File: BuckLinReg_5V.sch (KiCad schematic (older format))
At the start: 41 parts, among them J1 Barrel_Jack, J2 Conn_01x02_Male, J3 Conn_01x02_Male, J4 Conn_01x02_Male, Q1 SQD40061EL, U1 TPS56339DDC, U2 LM1085-5.0

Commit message: Added overcurrent protection circuit and assigned all MFPNs and footprints
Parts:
- added C12, C13, C14, C4: 0.1u, Capacitor_SMD:C_0603_1608Metric_Pad1.08x0.95mm_HandSolder, symbol Device:C_Small
- added D4: 3.0, Diode_SMD:D_SOD-323, symbol Device:D_Zener
- added D5: YELLOW, Diode_SMD:D_1206_3216Metric_Pad1.42x1.75mm_HandSolder, symbol Device:LED
- added Q1: PMBT2222, Package_TO_SOT_SMD:SOT-23_Handsoldering, symbol Device:Q_NPN_BEC
- added R10, R18, R2: 10k, Resistor_SMD:R_1206_3216Metric_Pad1.30x1.75mm_HandSolder, symbol Device:R
- added R11, R12: 1k, Resistor_SMD:R_1206_3216Metric_Pad1.30x1.75mm_HandSolder, symbol Device:R
- added R13, R14, R16: 100k, Resistor_SMD:R_1206_3216Metric_Pad1.30x1.75mm_HandSolder, symbol Device:R
- added R17: 12k, Resistor_SMD:R_1206_3216Metric_Pad1.30x1.75mm_HandSolder, symbol Device:R
- added SW1: SW_SPDT, Connector_PinHeader_2.54mm:PinHeader_1x03_P2.54mm_Vertical, symbol Switch:SW_SPDT
- added U1: TLV76050DBZT, Package_TO_SOT_SMD:SOT-23_Handsoldering, symbol BuckLinReg_5V:TLV76050DBZT
- added U2: LMV358, Package_SO:SOIC-8_3.9x4.9mm_P1.27mm, symbol Amplifier_Operational:LMV358
- added U3: 74HCT00, Package_SO:SOIC-14_3.9x8.7mm_P1.27mm, symbol 74xx:74LS00
- added U4: SN74HCT02, Package_SO:SOIC-14_3.9x8.7mm_P1.27mm, symbol 74xx:74LS02
- added U5: TCM810, Package_TO_SOT_SMD:SOT-23_Handsoldering, symbol Power_Supervisor:TCM810
- J2: renamed from J3; value Conn_01x02_Male -> 1x2 Male
- J3: renamed from J4; value Conn_01x02_Male -> 1x2 Male
- J4: renamed from J2; value Conn_01x02_Male -> 1x2 Male
- R8: renamed from R6; value 36k -> 68k; MFPN RMCF1206FT36K0 -> RMCF1206JT68K0
- R9: renamed from R7; value 4.7k -> 33k; MFPN RMCF1206FT4K70 -> RMCF1206JT33K0
- U7: renamed from U2; value LM1085-5.0 -> LM1084-5.0
- renumbered C9 to C10, C10 to C11, C4 to C5, C5 to C6, C6 to C7, C7 to C8, C8 to C9, D3 to D1, D1 to D3, Q1 to Q2, R8 to R1, R9 to R15, R1 to R3, R2 to R4, R4 to R5, R5 to R6, R3 to R7, TP2 to TP1, TP3 to TP2, TP1 to TP3, U1 to U6
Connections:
- net labels added: +Vin, 5V0_LOGIC, 5V0_Out, OCP_TRIGGER, POR, Q, S, SR+, SR-, SW_SIG, Vo, ~PWR_EN, ~Q, ~SW_SIG
- net labels removed: CapNode, U1Vin, U2Vin, Vout
- wire segments 121 -> 238
- no-connect marks 0 -> 2
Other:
- note added: "R"
- note added: "S"
- note added: "TPS56339 has a 5 ms soft-start\nWe must assert a definite EN voltage by t = 2 ms after power-up"
- note added: "Vo= (100k/1k) * ( (SR+) - (SR-) )"
- moved on the sheet: C1, C10, C11, C2, C3, C5, C6, C7, C8, C9, D1, D2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

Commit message: Two grounds: GNDA and pwrGND.  Continued PCB dev.
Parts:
- added NT1: Net-Tie_2, NetTie:NetTie-2_SMD_Pad0.5mm, symbol Device:Net-Tie_2
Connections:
- net labels added: DFA+, DFA-, GNDA, GNDPWR
- wire segments 238 -> 241
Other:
- moved on the sheet: R11, R12

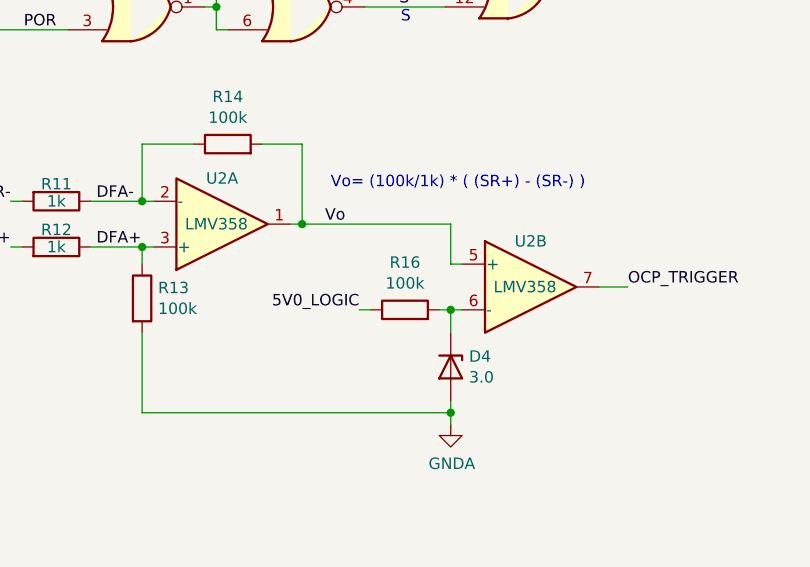
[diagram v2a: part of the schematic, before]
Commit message: Simulated zener for different values R.  Routed logic portion of board.
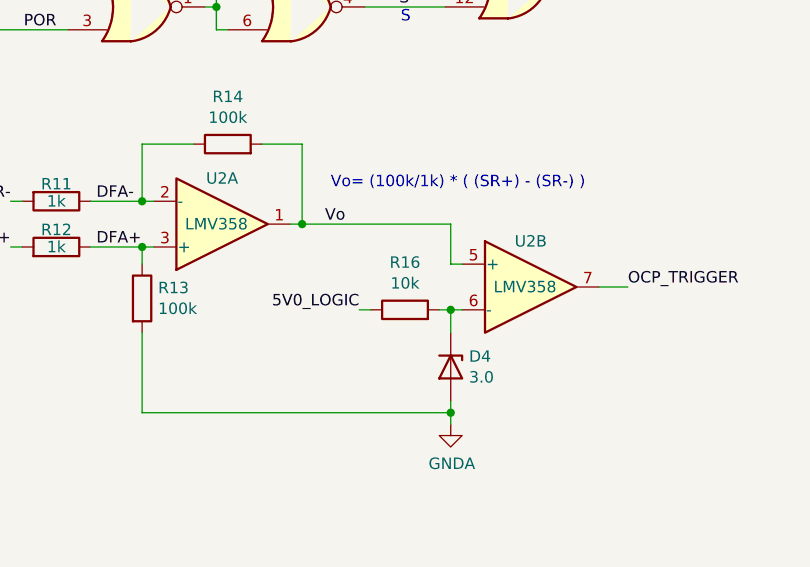
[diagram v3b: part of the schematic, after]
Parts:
- R16: value 100k -> 10k; MFPN RMCF1206JG100K -> RMCF1206JT10K0
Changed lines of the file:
@@
 P 7175 9250
 F 0 "R16" V 7382 9250 50  0000 C CNN
-F 1 "100k" V 7291 9250 50  0000 C CNN
+F 1 "10k" V 7291 9250 50  0000 C CNN
 F 2 "Resistor_SMD:R_1206_3216Metric_Pad1.30x1.75mm_HandSolder" V 7105 9250 50  0001 C CNN
 F 3 "~" H 7175 9250 50  0001 C CNN
-F 4 "RMCF1206JG100K" H 7175 9250 50  0001 C CNN "MFPN"
+F 4 "RMCF1206JT10K0" H 7175 9250 50  0001 C CNN "MFPN"
 	1    7175 9250
 	0    -1   -1   0
@@
 F 1 "LM1084-5.0" H 10500 4301 50  0000 C CNN
 F 2 "Package_TO_SOT_SMD:TO-263-3_TabPin2" H 10500 4400 50  0001 C CIN
-F 3 "http://www.ti.com/lit/ds/symlink/lm1085.pdf" H 10500 4150 50  0001 C CNN
+F 3 "http://www.ti.com/general/docs/suppproductinfo.tsp?distId=10&gotoUrl=http%3A%2F%2Fwww.ti.com%2Flit%2Fgpn%2Flm1084" H 10500 4150 50  0001 C CNN
 F 4 "LM1084ISX-5.0/NOPB" H 10500 4150 50  0001 C CNN "MFPN"
 	1    10500 4150
@@
 $EndComp
 $Comp
-L power:GNDA #PWR?
+L power:GNDA #PWR0106
 U 1 1 60668381
 P 2700 10075
-F 0 "#PWR?" H 2700 9825 50  0001 C CNN
+F 0 "#PWR0106" H 2700 9825 50  0001 C CNN
 F 1 "GNDA" H 2705 9902 50  0000 C CNN
 F 2 "" H 2700 10075 50  0001 C CNN
@@
 $EndComp
 $Comp
-L power:GNDA #PWR?
+L power:GNDA #PWR0108
 U 1 1 60698D68
 P 7975 6775
-F 0 "#PWR?" H 7975 6525 50  0001 C CNN
+F 0 "#PWR0108" H 7975 6525 50  0001 C CNN
 F 1 "GNDA" H 7980 6602 50  0000 C CNN
 F 2 "" H 7975 6775 50  0001 C CNN

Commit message: Added testpoints and finished routing board
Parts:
- removed J2: 1x2 Male, Connector_PinHeader_2.54mm:PinHeader_1x02_P2.54mm_Vertical, symbol Connector:Conn_01x02_Male
- removed TP2: EN, TestPoint:TestPoint_THTPad_D2.0mm_Drill1.0mm, symbol Connector:TestPoint
- removed TP5: BOOT, TestPoint:TestPoint_THTPad_D2.0mm_Drill1.0mm, symbol Connector:TestPoint
- added TP10: SR+, TestPoint:TestPoint_THTPad_D2.0mm_Drill1.0mm, symbol Connector:TestPoint
- added TP12: Q, TestPoint:TestPoint_THTPad_D2.0mm_Drill1.0mm, symbol Connector:TestPoint
- added TP13: Iout, TestPoint:TestPoint_THTPad_D2.0mm_Drill1.0mm, symbol Connector:TestPoint
- added TP14: ~Q, TestPoint:TestPoint_THTPad_D2.0mm_Drill1.0mm, symbol Connector:TestPoint
- added TP15: OCPT, TestPoint:TestPoint_THTPad_D2.0mm_Drill1.0mm, symbol Connector:TestPoint
- added TP16: GNDP, TestPoint:TestPoint_THTPad_D2.0mm_Drill1.0mm, symbol Connector:TestPoint
- added TP17: GNDA, TestPoint:TestPoint_THTPad_D2.0mm_Drill1.0mm, symbol Connector:TestPoint
- added TP8: ~PWR_EN, TestPoint:TestPoint_THTPad_D2.0mm_Drill1.0mm, symbol Connector:TestPoint
- added TP9: 5V0, TestPoint:TestPoint_THTPad_D2.0mm_Drill1.0mm, symbol Connector:TestPoint
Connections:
- net labels removed: GND
- wire segments 241 -> 251
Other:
- moved on the sheet: R16, TP7
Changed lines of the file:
@@
 	6850 4450 6800 4450
-Wire Wire Line
-	5675 4250 5925 4250
 Wire Wire Line
 	6200 4250 6200 4450
@@
 	6850 4100 6850 4150
 Wire Wire Line
-	5925 4300 5925 4250
-Connection ~ 5925 4250
-Wire Wire Line
-	5925 4250 6200 4250
-Wire Wire Line
 	5750 4625 5750 4575
 Connection ~ 5750 4575
@@
 	5750 4575 7000 4575
 Wire Wire Line
-	8025 4100 8025 4150
+	10150 4100 10150 4150
 Wire Wire Line
 	13825 1275 13825 1325
@@
 	15325 1375 15325 1325
 Connection ~ 15325 1325
-$Comp
-L power:GND #PWR05
-U 1 1 60224C3B
-P 8450 3850
-F 0 "#PWR05" H 8450 3600 50  0001 C CNN
-F 1 "GND" H 8455 3677 50  0000 C CNN
-F 2 "" H 8450 3850 50  0001 C CNN
-F 3 "" H 8450 3850 50  0001 C CNN
-	1    8450 3850
-	1    0    0    -1
-$EndComp
-Wire Wire Line
-	8450 3850 8450 3775
-Wire Wire Line
-	8350 3775 8350 4150
 Wire Wire Line
 	11250 4250 10800 4250
@@
 	4475 4575 4475 4625
 Wire Wire Line
-	4825 4575 4825 4625
-Wire Wire Line
 	3925 5025 3925 5075
 Wire Wire Line
@@
 Wire Wire Line
 	4825 4350 4825 4575
-Connection ~ 4825 4575
 Wire Wire Line
 	9025 4150 9225 4150
@@
 Connection ~ 9925 4150
 Wire Wire Line
-	9925 4150 10200 4150
+	9925 4150 10150 4150
 Wire Wire Line
 	9525 3775 9525 3825
@@
 	9225 4150 9425 4150
 Wire Wire Line
-	3275 4825 3225 4825
+	3275 4825 3200 4825
 Wire Wire Line
 	3575 4825 3625 4825
-Text Label 3225 4825 2    50   ~ 0
+Text Label 3125 4825 2    50   ~ 0
 ~PWR_EN
 Wire Wire Line
@@
 Wire Wire Line
 	3275 7475 4425 7475
-Wire Wire Line
-	4825 8025 5700 8025
 NoConn ~ 3350 9925
 NoConn ~ 3350 9375
@@
 Text Label 5650 7825 2    50   ~ 0
 OCP_TRIGGER
-Text Label 8150 9150 0    50   ~ 0
+Text Label 8175 9150 0    50   ~ 0
 OCP_TRIGGER
-Wire Wire Line
-	8025 9150 8150 9150
-Text Notes 6850 8725 0    50   ~ 0
+Text Notes 6850 8600 0    50   ~ 0
 Vo= (100k/1k) * ( (SR+) - (SR-) )
 Text Label 6825 8875 0    50   ~ 0
@@
 Wire Wire Line
 	7375 9700 7375 9750
-Text Label 6975 9250 2    50   ~ 0
+Text Label 6725 9250 2    50   ~ 0
 5V0_LOGIC
 Wire Wire Line
-	7025 9250 6975 9250
+	6775 9250 6725 9250
 Connection ~ 7375 9250
-Wire Wire Line
-	7325 9250 7375 9250
 Wire Wire Line
 	7375 9700 7375 9650
@@
 Wire Wire Line
 	3275 7525 3275 7475
-Text Label 7300 7250 2    50   ~ 0
+Text Label 7250 7250 2    50   ~ 0
 Q
 Text Label 8000 7825 0    50   ~ 0
@@
 	8000 7825 7950 7825
 Wire Wire Line
-	8000 7350 8000 7825
+	8000 7350 8000 7650
 Wire Wire Line
 	7950 7350 8000 7350
@@
 L Device:R R16
 U 1 1 606BFCCF
-P 7175 9250
-F 0 "R16" V 7382 9250 50  0000 C CNN
-F 1 "10k" V 7291 9250 50  0000 C CNN
-F 2 "Resistor_SMD:R_1206_3216Metric_Pad1.30x1.75mm_HandSolder" V 7105 9250 50  0001 C CNN
-F 3 "~" H 7175 9250 50  0001 C CNN
-F 4 "RMCF1206JT10K0" H 7175 9250 50  0001 C CNN "MFPN"
-	1    7175 9250
+P 6925 9250
+F 0 "R16" V 7132 9250 50  0000 C CNN
+F 1 "10k" V 7041 9250 50  0000 C CNN
+F 2 "Resistor_SMD:R_1206_3216Metric_Pad1.30x1.75mm_HandSolder" V 6855 9250 50  0001 C CNN
+F 3 "~" H 6925 9250 50  0001 C CNN
+F 4 "RMCF1206JT10K0" H 6925 9250 50  0001 C CNN "MFPN"
+	1    6925 9250
 	0    -1   -1   0
 $EndComp
@@
 $EndComp
 $Comp
-L Connector:Conn_01x02_Male J2
-U 1 1 602D0CD5
-P 8450 3575
-F 0 "J2" V 8325 3525 50  0000 C CNN
-F 1 "1x2 Male" V 8400 3525 50  0000 C CNN
-F 2 "Connector_PinHeader_2.54mm:PinHeader_1x02_P2.54mm_Vertical" H 8450 3575 50  0001 C CNN
-F 3 "~" H 8450 3575 50  0001 C CNN
-	1    8450 3575
-	0    1    1    0
-$EndComp
-$Comp
 L Connector:TestPoint TP7
 U 1 1 602C562C
-P 8025 4100
-F 0 "TP7" H 8083 4218 50  0000 L CNN
-F 1 "U2Vin" H 8083 4127 50  0000 L CNN
-F 2 "TestPoint:TestPoint_THTPad_D2.0mm_Drill1.0mm" H 8225 4100 50  0001 C CNN
-F 3 "~" H 8225 4100 50  0001 C CNN
-	1    8025 4100
+P 10150 4100
+F 0 "TP7" H 10208 4218 50  0000 L CNN
+F 1 "U2Vin" H 10208 4127 50  0000 L CNN
+F 2 "TestPoint:TestPoint_THTPad_D2.0mm_Drill1.0mm" H 10350 4100 50  0001 C CNN
+F 3 "~" H 10350 4100 50  0001 C CNN
+	1    10150 4100
 	-1   0    0    -1
 $EndComp
@@
 $EndComp
 $Comp
-L Connector:TestPoint TP5
-U 1 1 602B47DC
-P 5925 4300
-F 0 "TP5" H 5983 4418 50  0000 L CNN
-F 1 "BOOT" H 5983 4327 50  0000 L CNN
-F 2 "TestPoint:TestPoint_THTPad_D2.0mm_Drill1.0mm" H 6125 4300 50  0001 C CNN
-F 3 "~" H 6125 4300 50  0001 C CNN
-	1    5925 4300
-	1    0    0    1
-$EndComp
-$Comp
 L Connector:TestPoint TP6
 U 1 1 602A9E21
@@
 	1    6850 4100
 	-1   0    0    -1
-$EndComp
-$Comp
-L Connector:TestPoint TP2
-U 1 1 6029636E
-P 4825 4625
-F 0 "TP2" H 4883 4743 50  0000 L CNN
-F 1 "EN" H 4883 4652 50  0000 L CNN
-F 2 "TestPoint:TestPoint_THTPad_D2.0mm_Drill1.0mm" H 5025 4625 50  0001 C CNN
-F 3 "~" H 5025 4625 50  0001 C CNN
-	1    4825 4625
-	1    0    0    1
 $EndComp
 $Comp
@@
 	1    0    0    -1
 $EndComp
+$Comp
+L Connector:TestPoint TP9
+U 1 1 603A9AA4
+P 3300 6325
+F 0 "TP9" H 3358 6443 50  0000 L CNN
+F 1 "5V0" H 3358 6352 50  0000 L CNN
+F 2 "TestPoint:TestPoint_THTPad_D2.0mm_Drill1.0mm" H 3500 6325 50  0001 C CNN
+F 3 "~" H 3500 6325 50  0001 C CNN
+	1    3300 6325
+	-1   0    0    -1
+$EndComp
+Wire Wire Line
+	3300 6325 3300 6375
+$Comp
+L Connector:TestPoint TP13
+U 1 1 603DB5D6
+P 7375 8825
+F 0 "TP13" H 7433 8943 50  0000 L CNN
+F 1 "Iout" H 7433 8852 50  0000 L CNN
+F 2 "TestPoint:TestPoint_THTPad_D2.0mm_Drill1.0mm" H 7575 8825 50  0001 C CNN
+F 3 "~" H 7575 8825 50  0001 C CNN
+	1    7375 8825
+	-1   0    0    -1
+$EndComp
+Wire Wire Line
+	7375 8825 7375 8875
+Connection ~ 7375 8875
+$Comp
+L Connector:TestPoint TP14
+U 1 1 604CB1A8
+P 8050 7650
+F 0 "TP14" H 8108 7768 50  0000 L CNN
+F 1 "~Q" H 8108 7677 50  0000 L CNN
+F 2 "TestPoint:TestPoint_THTPad_D2.0mm_Drill1.0mm" H 8250 7650 50  0001 C CNN
+F 3 "~" H 8250 7650 50  0001 C CNN
+	1    8050 7650
+	0    1    -1   0
+$EndComp
+Wire Wire Line
+	8050 7650 8000 7650
+Connection ~ 8000 7650
+Wire Wire Line
+	8000 7650 8000 7825
+$Comp
+L Connector:TestPoint TP12
+U 1 1 604EEC3C
+P 7300 7150
+F 0 "TP12" H 7358 7268 50  0000 L CNN
+F 1 "Q" H 7358 7177 50  0000 L CNN
+F 2 "TestPoint:TestPoint_THTPad_D2.0mm_Drill1.0mm" H 7500 7150 50  0001 C CNN
+F 3 "~" H 7500 7150 50  0001 C CNN
+	1    7300 7150
+	-1   0    0    -1
+$EndComp
+Wire Wire Line
+	7300 7250 7300 7150
+$Comp
+L Connector:TestPoint TP8
+U 1 1 605351DA
+P 3200 4700
+F 0 "TP8" H 3258 4818 50  0000 L CNN
+F 1 "~PWR_EN" H 3258 4727 50  0000 L CNN
+F 2 "TestPoint:TestPoint_THTPad_D2.0mm_Drill1.0mm" H 3400 4700 50  0001 C CNN
+F 3 "~" H 3400 4700 50  0001 C CNN
+	1    3200 4700
+	-1   0    0    -1
+$EndComp
+Wire Wire Line
+	3200 4700 3200 4825
+Connection ~ 3200 4825
+Wire Wire Line
+	3200 4825 3125 4825
+$Comp
+L Connector:TestPoint TP15
+U 1 1 6056A5D9
+P 8100 9000
+F 0 "TP15" H 8158 9118 50  0000 L CNN
+F 1 "OCPT" H 8158 9027 50  0000 L CNN
+F 2 "TestPoint:TestPoint_THTPad_D2.0mm_Drill1.0mm" H 8300 9000 50  0001 C CNN
+F 3 "~" H 8300 9000 50  0001 C CNN
+	1    8100 9000
+	-1   0    0    -1
+$EndComp
+Wire Wire Line
+	8100 9000 8100 9150
+Connection ~ 8100 9150
+Wire Wire Line
+	8100 9150 8175 9150
+Wire Wire Line
+	8025 9150 8100 9150
+$Comp
+L Connector:TestPoint TP17
+U 1 1 60602B24
+P 1575 5700
+F 0 "TP17" H 1633 5818 50  0000 L CNN
+F 1 "GNDA" H 1633 5727 50  0000 L CNN
+F 2 "TestPoint:TestPoint_THTPad_D2.0mm_Drill1.0mm" H 1775 5700 50  0001 C CNN
+F 3 "~" H 1775 5700 50  0001 C CNN
+	1    1575 5700
+	-1   0    0    -1
+$EndComp
+$Comp
+L Connector:TestPoint TP16
+U 1 1 60614592
+P 825 5700
+F 0 "TP16" H 883 5818 50  0000 L CNN
+F 1 "GNDP" H 883 5727 50  0000 L CNN
+F 2 "TestPoint:TestPoint_THTPad_D2.0mm_Drill1.0mm" H 1025 5700 50  0001 C CNN
+F 3 "~" H 1025 5700 50  0001 C CNN
+	1    825  5700
+	-1   0    0    -1
+$EndComp
+Wire Wire Line
+	825  5700 825  5750
+Wire Wire Line
+	825  5750 950  5750
+Connection ~ 950  5750
+Wire Wire Line
+	1250 5750 1575 5750
+Wire Wire Line
+	1575 5750 1575 5700
+Connection ~ 1250 5750
+Wire Wire Line
+	4825 8025 5700 8025
+Connection ~ 10150 4150
+Wire Wire Line
+	10150 4150 10200 4150
+Wire Wire Line
+	8675 4100 8675 4150
+$Comp
+L Connector:TestPoint TP10
+U 1 1 606CEE09
+P 8675 4100
+F 0 "TP10" H 8733 4218 50  0000 L CNN
+F 1 "SR+" H 8733 4127 50  0000 L CNN
+F 2 "TestPoint:TestPoint_THTPad_D2.0mm_Drill1.0mm" H 8875 4100 50  0001 C CNN
+F 3 "~" H 8875 4100 50  0001 C CNN
+	1    8675 4100
+	-1   0    0    -1
+$EndComp
+Wire Wire Line
+	7075 9250 7375 9250
+Wire Wire Line
+	5675 4250 6200 4250
 $EndSCHEMATC

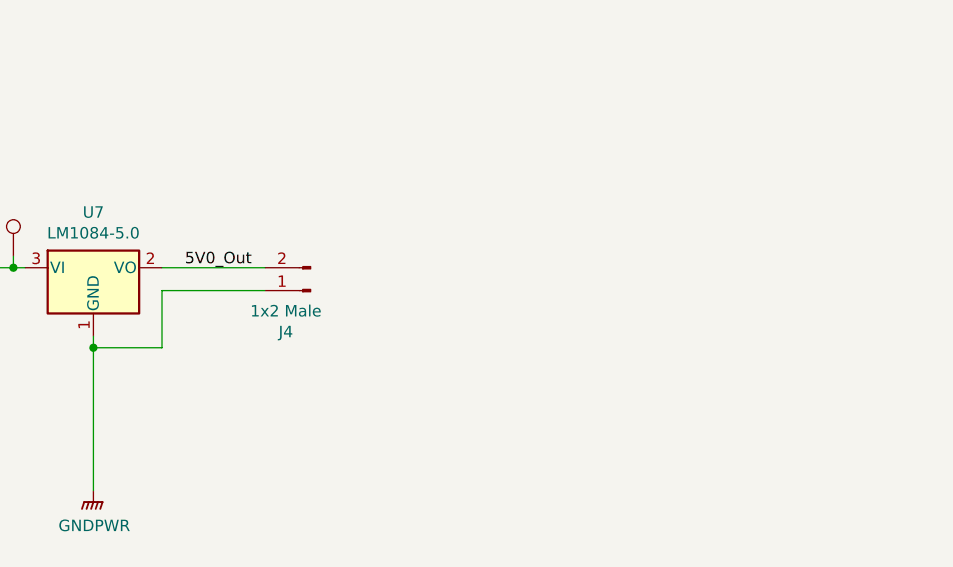
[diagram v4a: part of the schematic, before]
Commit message: Added new power barrier connector.  Increased minimum copper to copper clearance to 0.21 mm.
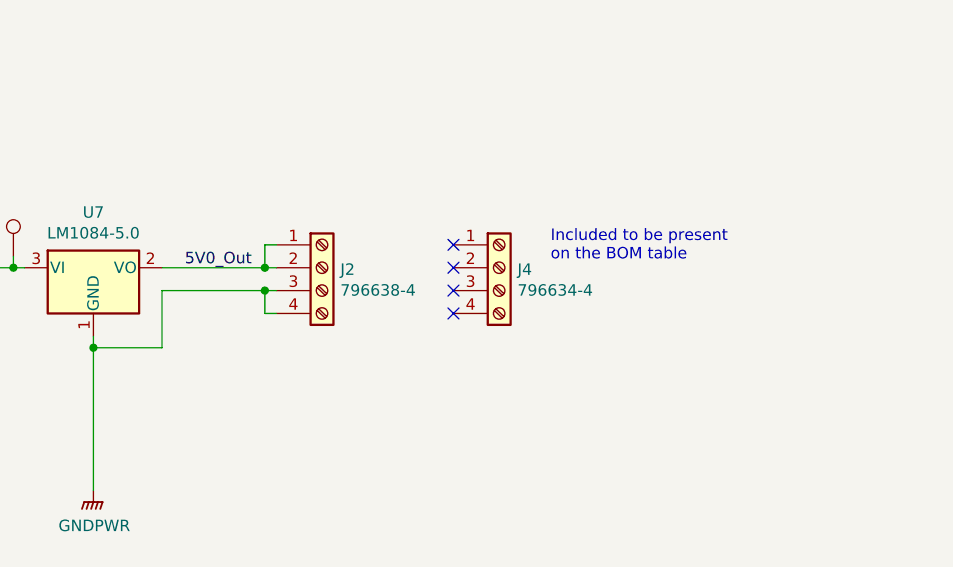
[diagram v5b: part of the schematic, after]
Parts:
- removed J4: 1x2 Male, Connector_PinHeader_2.54mm:PinHeader_1x02_P2.54mm_Vertical, symbol Connector:Conn_01x02_Male
- added J2: 796638-4, BuckLinReg_5V:796636-4, symbol Connector:Screw_Terminal_01x04
- added J4: 796634-4, symbol Connector:Screw_Terminal_01x04
- NT1: footprint NetTie:NetTie-2_SMD_Pad0.5mm -> BuckLinReg_5V:NetShorter
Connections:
- net 5V0_Out: now also J2.1 (Pin_1), J2.2 (Pin_2)
- net GNDPWR: now also J2.3 (Pin_3), J2.4 (Pin_4)
- no-connect marks 2 -> 6
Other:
- note added: "Included to be present\non the BOM table"
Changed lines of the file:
@@
 Connection ~ 15325 1325
-Wire Wire Line
-	11250 4250 10800 4250
-Wire Wire Line
-	10800 4150 11250 4150
 Wire Wire Line
 	9725 4150 9925 4150
@@
 $EndComp
 $Comp
-L Connector:Conn_01x02_Male J4
-U 1 1 602CABE2
-P 11450 4250
-F 0 "J4" H 11558 4431 50  0000 C CNN
-F 1 "1x2 Male" H 11558 4340 50  0000 C CNN
-F 2 "Connector_PinHeader_2.54mm:PinHeader_1x02_P2.54mm_Vertical" H 11450 4250 50  0001 C CNN
-F 3 "~" H 11450 4250 50  0001 C CNN
-	1    11450 4250
-	-1   0    0    1
-$EndComp
-$Comp
 L Device:R R15
 U 1 1 60243959
@@
 F 0 "NT1" H 1100 5931 50  0000 C CNN
 F 1 "Net-Tie_2" H 1100 5840 50  0000 C CNN
-F 2 "NetTie:NetTie-2_SMD_Pad0.5mm" H 1100 5750 50  0001 C CNN
+F 2 "BuckLinReg_5V:NetShorter" H 1100 5750 50  0001 C CNN
 F 3 "~" H 1100 5750 50  0001 C CNN
 	1    1100 5750
@@
 Wire Wire Line
 	5675 4250 6200 4250
+$Comp
+L Connector:Screw_Terminal_01x04 J2
+U 1 1 603C2A20
+P 11500 4150
+F 0 "J2" H 11580 4142 50  0000 L CNN
+F 1 "796638-4" H 11580 4051 50  0000 L CNN
+F 2 "BuckLinReg_5V:796636-4" H 11500 4150 50  0001 C CNN
+F 3 "~" H 11500 4150 50  0001 C CNN
+	1    11500 4150
+	1    0    0    -1
+$EndComp
+Wire Wire Line
+	10800 4150 11250 4150
+Wire Wire Line
+	11250 4150 11250 4050
+Wire Wire Line
+	11250 4050 11300 4050
+Connection ~ 11250 4150
+Wire Wire Line
+	11250 4150 11300 4150
+Wire Wire Line
+	10800 4250 11250 4250
+Wire Wire Line
+	11250 4250 11250 4350
+Wire Wire Line
+	11250 4350 11300 4350
+Connection ~ 11250 4250
+Wire Wire Line
+	11250 4250 11300 4250
+$Comp
+L Connector:Screw_Terminal_01x04 J4
+U 1 1 6040F530
+P 12275 4150
+F 0 "J4" H 12355 4142 50  0000 L CNN
+F 1 "796634-4" H 12355 4051 50  0000 L CNN
+F 2 "" H 12275 4150 50  0001 C CNN
+F 3 "~" H 12275 4150 50  0001 C CNN
+	1    12275 4150
+	1    0    0    -1
+$EndComp
+NoConn ~ 12075 4050
+NoConn ~ 12075 4150
+NoConn ~ 12075 4250
+NoConn ~ 12075 4350
+Text Notes 12500 4125 0    50   ~ 0
+Included to be present\non the BOM table
 $EndSCHEMATC
